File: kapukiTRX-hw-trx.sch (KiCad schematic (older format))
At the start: 26 parts, among them J1 GPS, J2 SWD, U1 STM32G474VE, U2 LP38693-3.3, Y1 16MHz

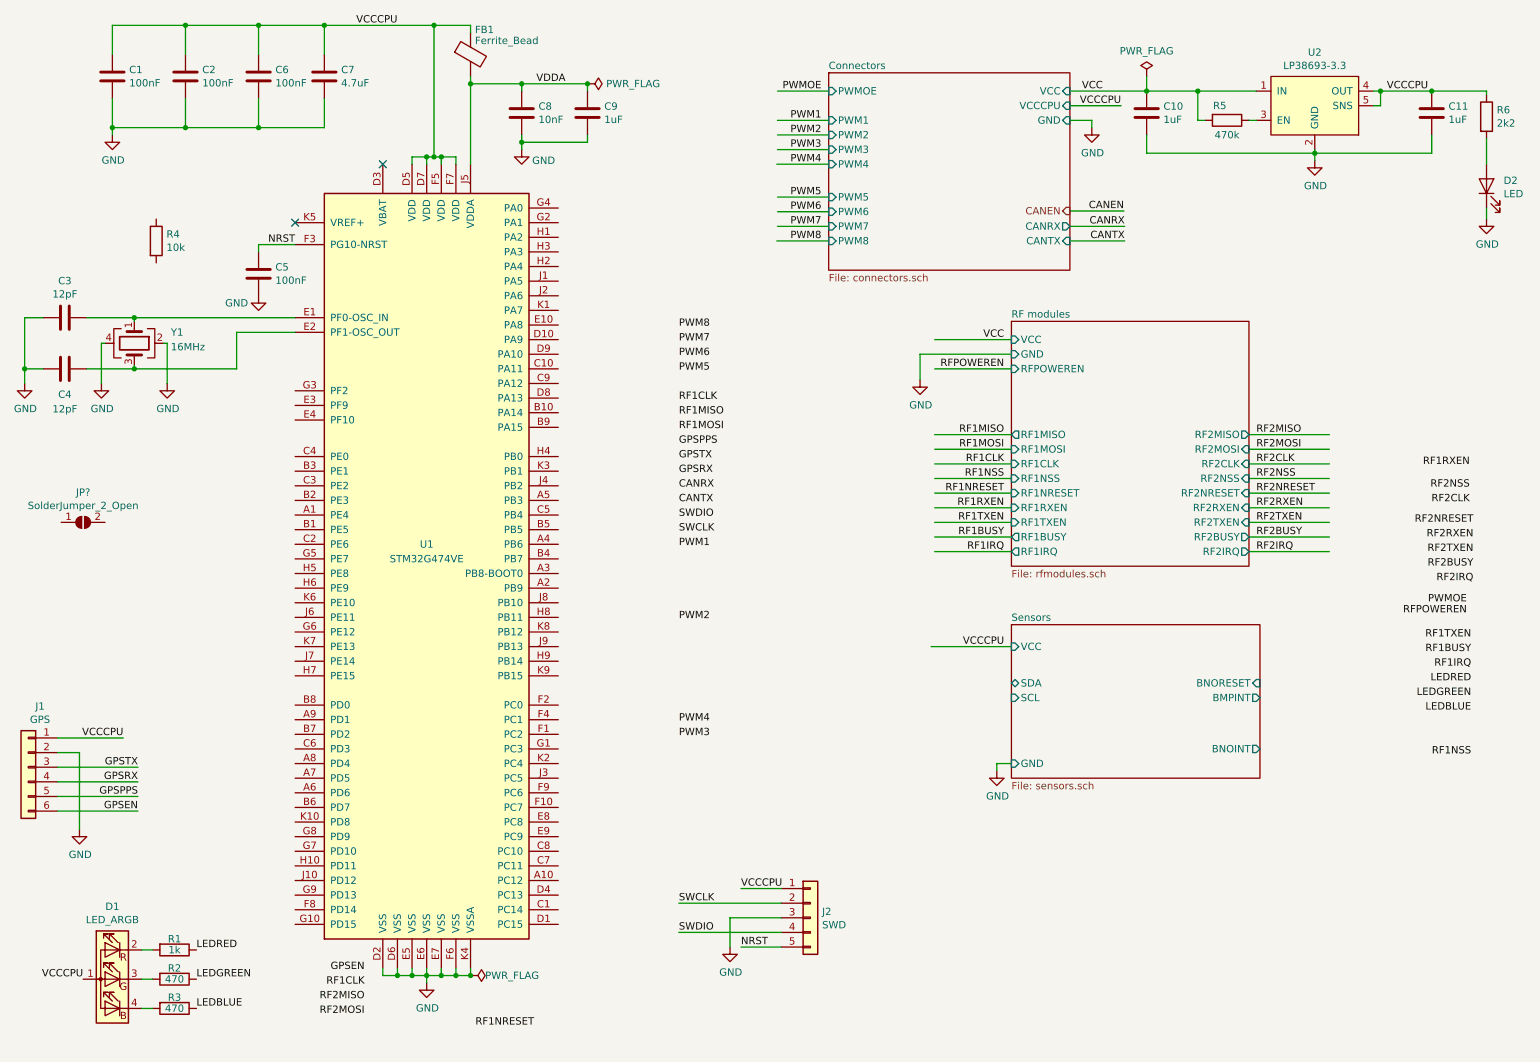
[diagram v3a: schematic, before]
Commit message: Add nets more nets
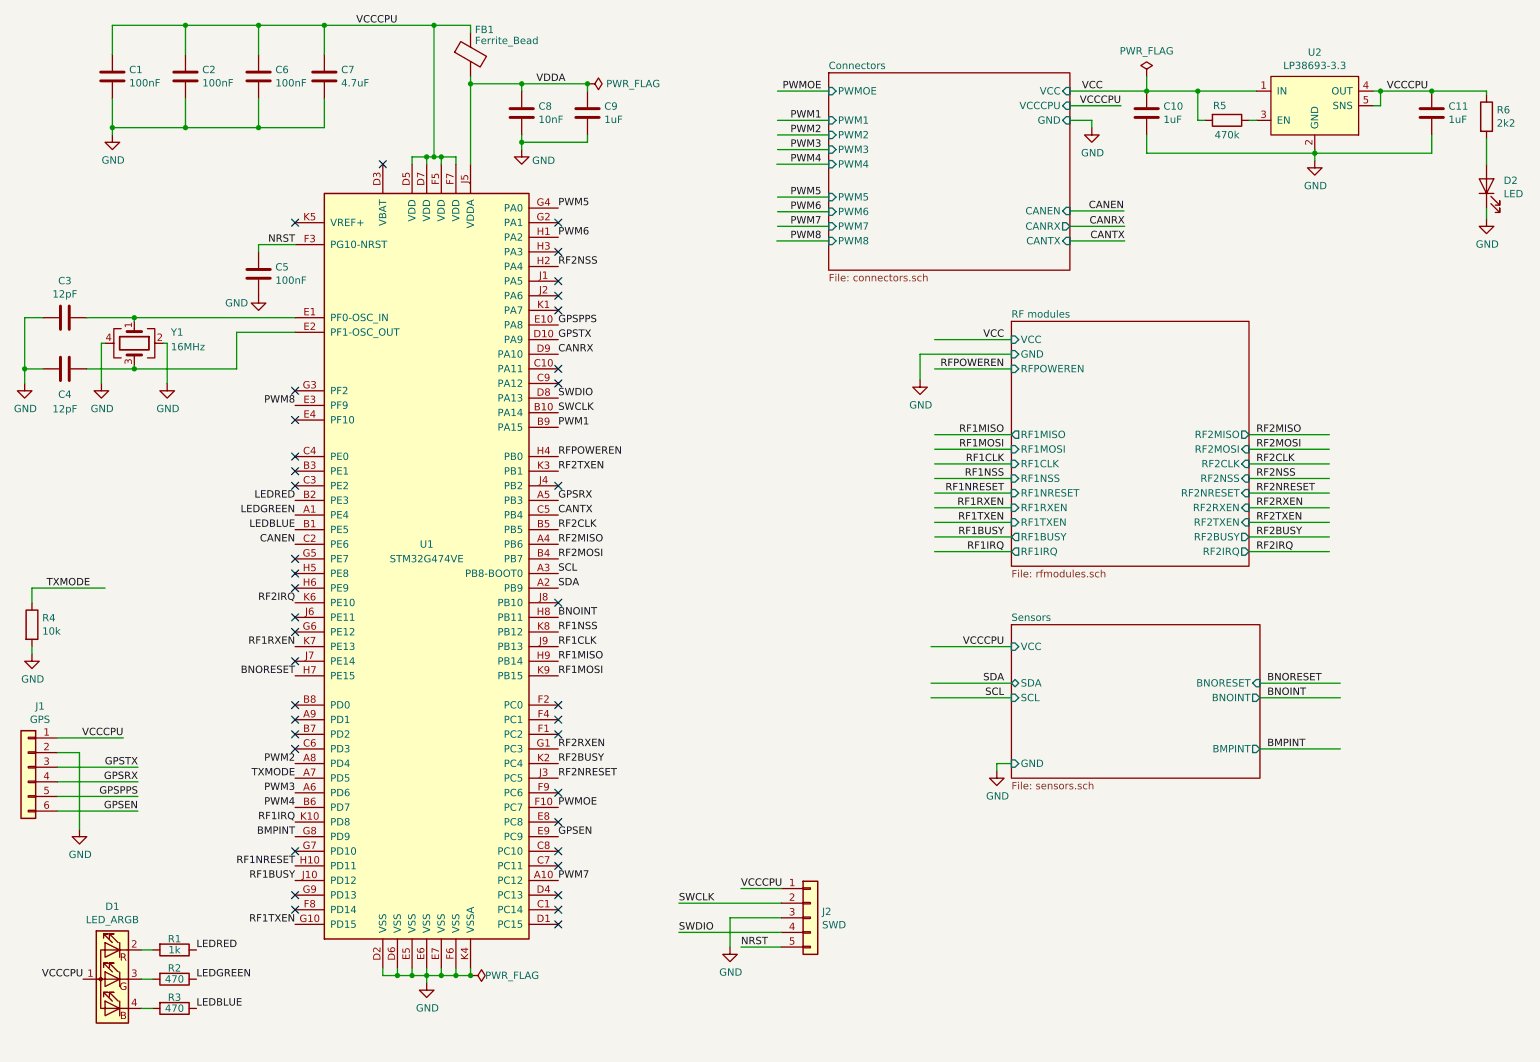
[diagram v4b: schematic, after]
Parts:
- removed JP?: SolderJumper_2_Open, symbol Jumper:SolderJumper_2_Open
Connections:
- net labels added: BMPINT, BNOINT, BNORESET, SCL, SDA, TXMODE
- wire segments 146 -> 154
- no-connect marks 2 -> 39
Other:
- moved on the sheet: R4
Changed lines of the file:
@@
 F14 "CANRX" O R 7950 2025 50
 F15 "CANTX" I R 7950 2125 50
+F16 "CANEN" I R 7950 1920 50
 $EndSheet
 Text Label 5275 6655 0    50   ~ 0
 SWCLK
-Text Label 5275 4725 0    50   ~ 0
+Text Label 2650 5700 2    50   ~ 0
 PWM2
-Text Label 5275 3325 0    50   ~ 0
+Text Label 4450 5000 0    50   ~ 0
 RF1MISO
-Text Label 5275 3425 0    50   ~ 0
+Text Label 4450 5100 0    50   ~ 0
 RF1MOSI
-Text Label 3125 7225 2    50   ~ 0
-RF1CLK
-$Comp
-L Device:R R4
-U 1 1 5C7B6C85
-P 1700 2125
-F 0 "R4" H 1770 2171 50  0000 L CNN
-F 1 "10k" H 1770 2080 50  0000 L CNN
-F 2 "Resistor_SMD:R_0402_1005Metric" V 1630 2125 50  0001 C CNN
-F 3 "~" H 1700 2125 50  0001 C CNN
-	1    1700 2125
-	1    0    0    -1
-$EndComp
+Text Label 4450 4700 0    50   ~ 0
+BNOINT
 $Sheet
 S 7550 2675 1625 1675
@@
 Text Label 6250 1100 2    50   ~ 0
 PWMOE
-Text Label 5275 4225 0    50   ~ 0
+Text Label 4450 3400 0    50   ~ 0
 PWM1
-Text Label 4285 7505 2    50   ~ 0
+Text Label 2650 6400 2    50   ~ 0
 RF1NRESET
-Text Label 10685 3670 2    50   ~ 0
+Text Label 2650 4900 2    50   ~ 0
 RF1RXEN
-Text Label 10695 4850 2    50   ~ 0
+Text Label 2650 6800 2    50   ~ 0
 RF1TXEN
-Text Label 10695 4950 2    50   ~ 0
+Text Label 2650 6500 2    50   ~ 0
 RF1BUSY
-Text Label 10695 5050 2    50   ~ 0
+Text Label 2650 6100 2    50   ~ 0
 RF1IRQ
-Text Label 10695 5650 2    50   ~ 0
+Text Label 4450 4800 0    50   ~ 0
 RF1NSS
-Text Label 10710 4065 2    50   ~ 0
+Text Label 4450 5800 0    50   ~ 0
 RF2NRESET
-Text Label 10710 4165 2    50   ~ 0
+Text Label 4450 5600 0    50   ~ 0
 RF2RXEN
-Text Label 10710 4265 2    50   ~ 0
+Text Label 4450 3700 0    50   ~ 0
 RF2TXEN
-Text Label 10710 4365 2    50   ~ 0
+Text Label 4450 5700 0    50   ~ 0
 RF2BUSY
-Text Label 10710 4465 2    50   ~ 0
+Text Label 2650 4600 2    50   ~ 0
 RF2IRQ
-Text Label 10665 4610 2    50   ~ 0
+Text Label 4450 6000 0    50   ~ 0
 PWMOE
-Text Label 10665 4685 2    50   ~ 0
+Text Label 4450 3600 0    50   ~ 0
 RFPOWEREN
 Text Label 7500 3000 2    50   ~ 0
 RFPOWEREN
-Text Label 3125 7325 2    50   ~ 0
+Text Label 4450 4200 0    50   ~ 0
 RF2MISO
-Text Label 10685 3925 2    50   ~ 0
+Text Label 4450 4100 0    50   ~ 0
 RF2CLK
-Text Label 5275 3925 0    50   ~ 0
+Text Label 4450 4000 0    50   ~ 0
 CANTX
-Text Label 10685 3825 2    50   ~ 0
+Text Label 4450 2300 0    50   ~ 0
 RF2NSS
 Wire Wire Line
@@
 Text Label 1975 7375 0    50   ~ 0
 LEDBLUE
-Text Label 10695 5150 2    50   ~ 0
+Text Label 2650 3900 2    50   ~ 0
 LEDRED
-Text Label 10695 5250 2    50   ~ 0
+Text Label 2650 4000 2    50   ~ 0
 LEDGREEN
-Text Label 10695 5350 2    50   ~ 0
+Text Label 2650 4100 2    50   ~ 0
 LEDBLUE
 Wire Wire Line
@@
 	0    1    1    0
 $EndComp
-Text Label 5275 3825 0    50   ~ 0
+Text Label 4450 2900 0    50   ~ 0
 CANRX
 Text Label 6250 1300 2    50   ~ 0
@@
 Text Label 5275 6855 0    50   ~ 0
 SWDIO
-Text Label 5275 4125 0    50   ~ 0
+Text Label 4450 3300 0    50   ~ 0
 SWCLK
-Text Label 5275 4025 0    50   ~ 0
+Text Label 4450 3200 0    50   ~ 0
 SWDIO
-Text Label 5275 2725 0    50   ~ 0
+Text Label 2650 3250 2    50   ~ 0
 PWM8
-Text Label 5275 2825 0    50   ~ 0
+Text Label 4450 6500 0    50   ~ 0
 PWM7
-Text Label 5275 2925 0    50   ~ 0
+Text Label 4450 2100 0    50   ~ 0
 PWM6
-Text Label 5275 3025 0    50   ~ 0
+Text Label 4450 1900 0    50   ~ 0
 PWM5
-Text Label 5275 3225 0    50   ~ 0
+Text Label 4450 4900 0    50   ~ 0
 RF1CLK
-Text Label 3125 7425 2    50   ~ 0
+Text Label 4450 4300 0    50   ~ 0
 RF2MOSI
-Text Label 5275 5425 0    50   ~ 0
+Text Label 2650 6000 2    50   ~ 0
 PWM4
-Text Label 5275 5525 0    50   ~ 0
+Text Label 2650 5900 2    50   ~ 0
 PWM3
-Text Label 5275 3725 0    50   ~ 0
+Text Label 4450 3900 0    50   ~ 0
 GPSRX
-Text Label 5275 3625 0    50   ~ 0
+Text Label 4450 2800 0    50   ~ 0
 GPSTX
-Text Label 5275 3525 0    50   ~ 0
+Text Label 4450 2700 0    50   ~ 0
 GPSPPS
-Text Label 3125 7125 2    50   ~ 0
+Text Label 4450 6200 0    50   ~ 0
 GPSEN
 Text Label 8320 1920 2    50   ~ 0
@@
 Wire Wire Line
 	7950 1920 8320 1920
-Text HLabel 7950 1920 0    50   Output ~ 0
-CANEN
 Text Label 7500 4900 2    50   ~ 0
 VCCCPU
@@
 F0 "Sensors" 50
 F1 "sensors.sch" 50
-F2 "BMPINT" O R 9250 5250 50
-F3 "BNOINT" O R 9250 5600 50
+F2 "BMPINT" O R 9250 5600 50
+F3 "BNOINT" O R 9250 5250 50
 F4 "BNORESET" I R 9250 5150 50
 F5 "GND" I L 7550 5700 50
@@
 	1    0    0    -1
 $EndComp
-$Comp
-L Jumper:SolderJumper_2_Open JP?
-U 1 1 5E0BD70F
-P 1200 4050
-F 0 "JP?" H 1200 4255 50  0000 C CNN
-F 1 "SolderJumper_2_Open" H 1200 4164 50  0000 C CNN
-F 2 "" H 1200 4050 50  0001 C CNN
-F 3 "~" H 1200 4050 50  0001 C CNN
-	1    1200 4050
-	1    0    0    -1
-$EndComp
+Text Label 4450 4500 0    50   ~ 0
+SDA
+Text Label 4450 4400 0    50   ~ 0
+SCL
+Text Label 7500 5150 2    50   ~ 0
+SDA
+Text Label 7500 5250 2    50   ~ 0
+SCL
+Wire Wire Line
+	7550 5150 7000 5150
+Wire Wire Line
+	7550 5250 7000 5250
+Text Label 2650 5100 2    50   ~ 0
+BNORESET
+Text Label 9300 5150 0    50   ~ 0
+BNORESET
+Wire Wire Line
+	9250 5150 9800 5150
+Text Label 9300 5250 0    50   ~ 0
+BNOINT
+Text Label 9300 5600 0    50   ~ 0
+BMPINT
+Wire Wire Line
+	9250 5250 9800 5250
+Wire Wire Line
+	9250 5600 9800 5600
+Text Label 2650 4200 2    50   ~ 0
+CANEN
+$Comp
+L Device:R R4
+U 1 1 5C7B6C85
+P 850 4750
+F 0 "R4" H 920 4796 50  0000 L CNN
+F 1 "10k" H 920 4705 50  0000 L CNN
+F 2 "Resistor_SMD:R_0402_1005Metric" V 780 4750 50  0001 C CNN
+F 3 "~" H 850 4750 50  0001 C CNN
+	1    850  4750
+	1    0    0    -1
+$EndComp
+$Comp
+L power:GND #PWR0112
+U 1 1 5DCBC9B2
+P 850 4950
+F 0 "#PWR0112" H 850 4700 50  0001 C CNN
+F 1 "GND" H 855 4777 50  0000 C CNN
+F 2 "" H 850 4950 50  0001 C CNN
+F 3 "" H 850 4950 50  0001 C CNN
+	1    850  4950
+	1    0    0    -1
+$EndComp
+Wire Wire Line
+	850  4950 850  4900
+Wire Wire Line
+	850  4600 850  4500
+Wire Wire Line
+	850  4500 1350 4500
+Text Label 950  4500 0    50   ~ 0
+TXMODE
+Text Label 2650 5800 2    50   ~ 0
+TXMODE
+NoConn ~ 2650 5300
+NoConn ~ 2650 5400
+NoConn ~ 2650 5500
+NoConn ~ 2650 5600
+NoConn ~ 2650 6300
+NoConn ~ 2650 5000
+NoConn ~ 2650 4800
+NoConn ~ 2650 4700
+NoConn ~ 2650 4500
+NoConn ~ 2650 4400
+NoConn ~ 2650 4300
+NoConn ~ 2650 3350
+NoConn ~ 2650 3150
+NoConn ~ 4450 2000
+NoConn ~ 4450 2200
+NoConn ~ 4450 2400
+NoConn ~ 4450 2500
+NoConn ~ 4450 2600
+NoConn ~ 4450 3000
+NoConn ~ 4450 3100
+NoConn ~ 4450 3800
+NoConn ~ 4450 4600
+NoConn ~ 4450 5300
+NoConn ~ 4450 5400
+NoConn ~ 4450 5500
+NoConn ~ 4450 5900
+NoConn ~ 4450 6100
+NoConn ~ 4450 6300
+NoConn ~ 4450 6400
+NoConn ~ 4450 6600
+NoConn ~ 4450 6700
+NoConn ~ 4450 6800
+NoConn ~ 2650 6700
+NoConn ~ 2650 6600
+NoConn ~ 2650 3600
+NoConn ~ 2650 3700
+NoConn ~ 2650 3800
+Text Label 2650 6200 2    50   ~ 0
+BMPINT
 $EndSCHEMATC

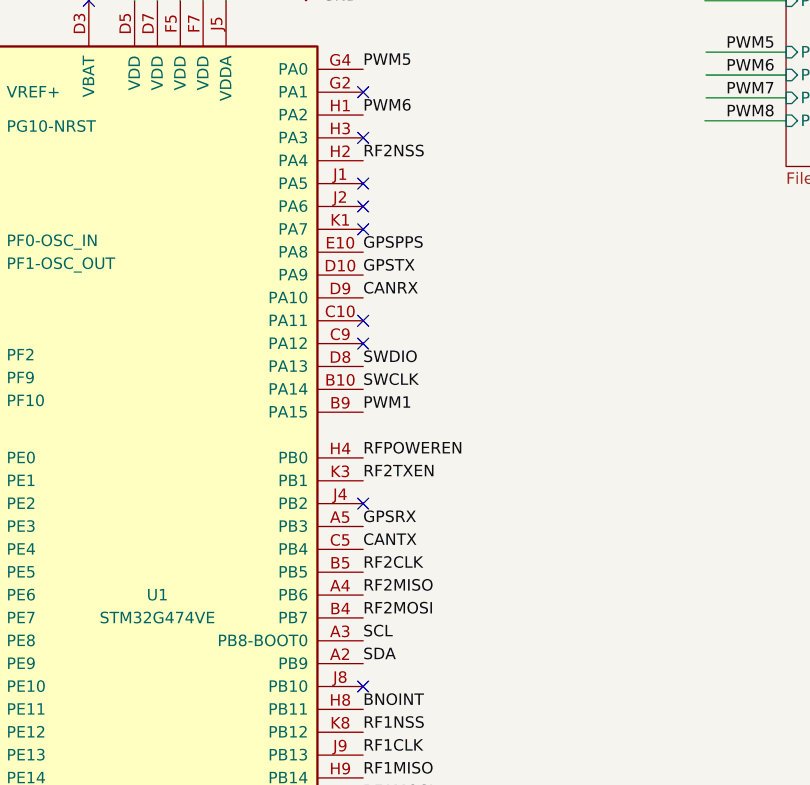
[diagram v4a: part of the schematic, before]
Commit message: Change some pins for better routing
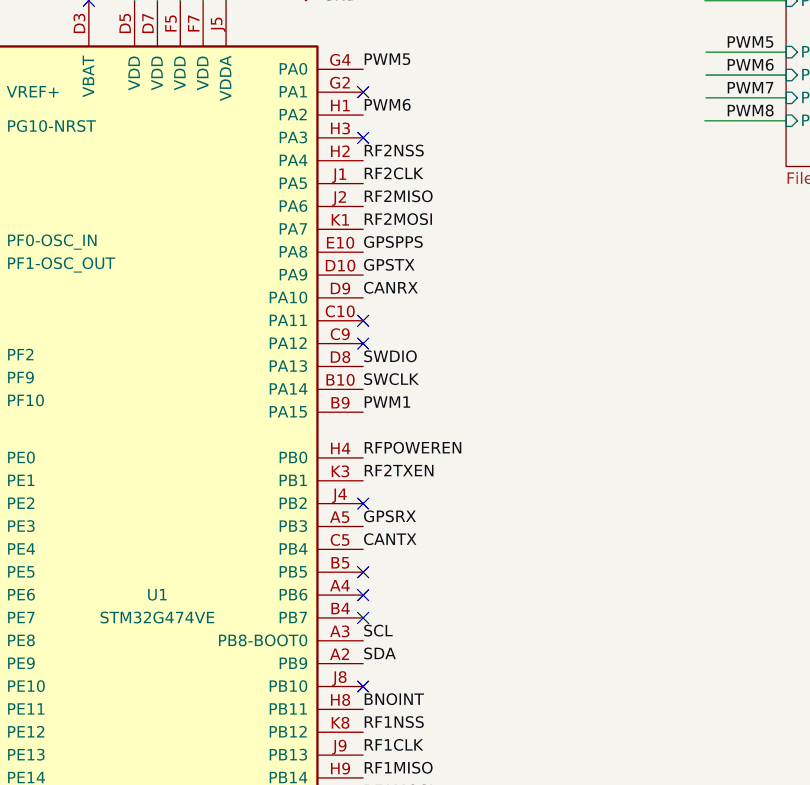
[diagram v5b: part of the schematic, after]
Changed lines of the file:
@@
 Text Label 7500 3000 2    50   ~ 0
 RFPOWEREN
-Text Label 4450 4200 0    50   ~ 0
+Text Label 4450 2500 0    50   ~ 0
 RF2MISO
-Text Label 4450 4100 0    50   ~ 0
+Text Label 4450 2400 0    50   ~ 0
 RF2CLK
 Text Label 4450 4000 0    50   ~ 0
@@
 Text Label 4450 4900 0    50   ~ 0
 RF1CLK
-Text Label 4450 4300 0    50   ~ 0
+Text Label 4450 2600 0    50   ~ 0
 RF2MOSI
 Text Label 2650 6000 2    50   ~ 0
@@
 NoConn ~ 4450 2000
 NoConn ~ 4450 2200
-NoConn ~ 4450 2400
-NoConn ~ 4450 2500
-NoConn ~ 4450 2600
+NoConn ~ 4450 4100
+NoConn ~ 4450 4200
+NoConn ~ 4450 4300
 NoConn ~ 4450 3000
 NoConn ~ 4450 3100

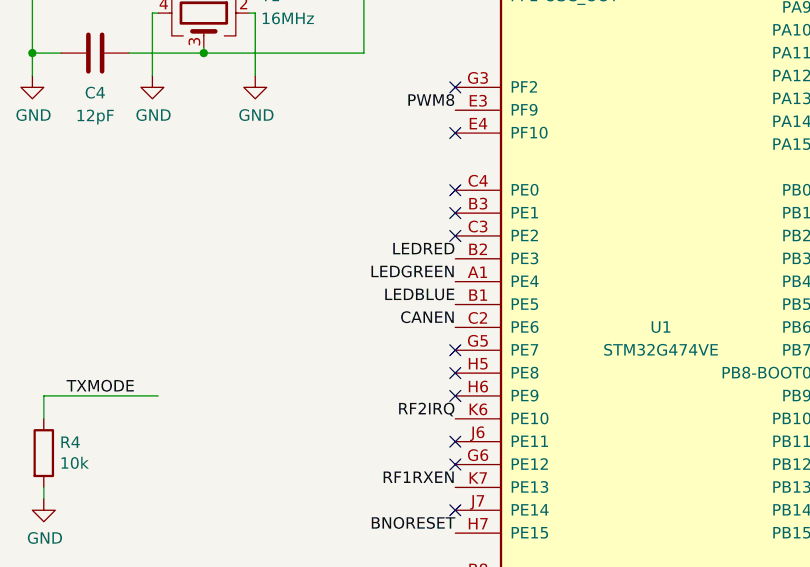
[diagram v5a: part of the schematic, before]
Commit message: Add proper footprint for BMP388
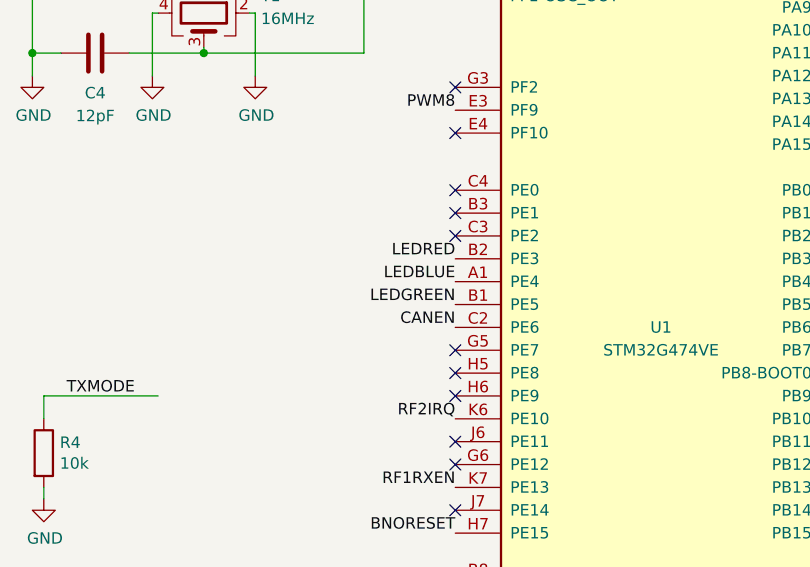
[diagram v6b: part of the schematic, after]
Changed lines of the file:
@@
 Text Label 2650 3900 2    50   ~ 0
 LEDRED
+Text Label 2650 4100 2    50   ~ 0
+LEDGREEN
 Text Label 2650 4000 2    50   ~ 0
-LEDGREEN
-Text Label 2650 4100 2    50   ~ 0
 LEDBLUE
 Wire Wire Line
